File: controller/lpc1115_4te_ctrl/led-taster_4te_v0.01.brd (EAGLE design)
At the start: 66.5 x 41 mm, 29 parts, among them IC1 74HC166D, T1 BC847, T2 BC847

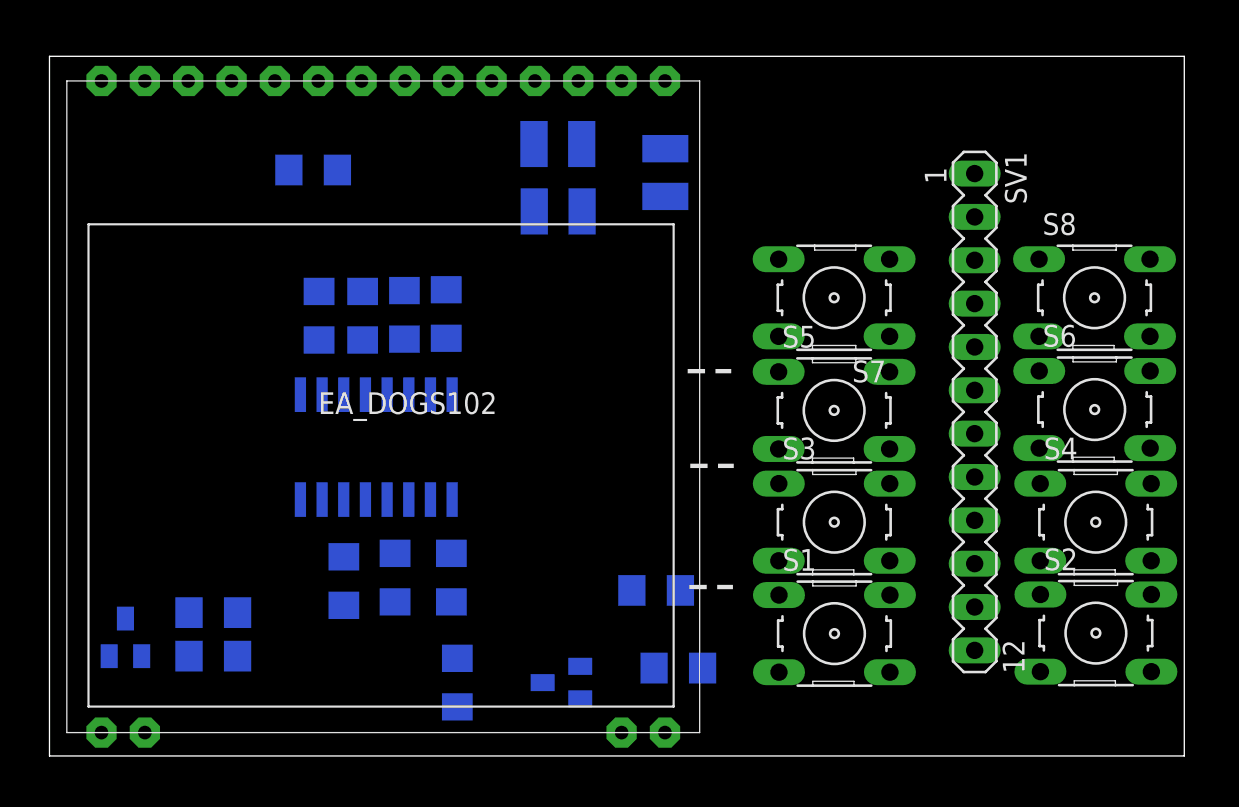
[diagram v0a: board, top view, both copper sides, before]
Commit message: LCD Taster PCB geroutet
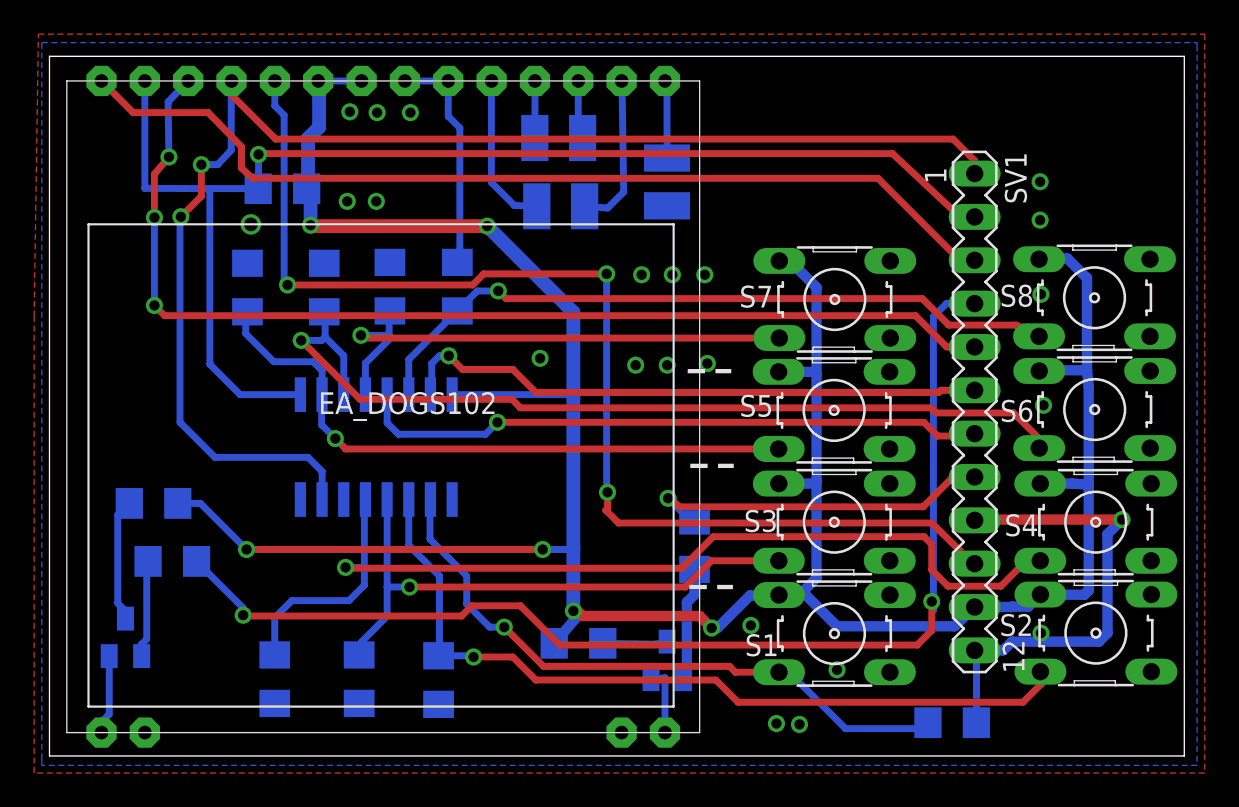
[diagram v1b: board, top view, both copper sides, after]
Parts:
- moved R2 19.0 mm to (52.9, 1.95), turned to 180 degrees
- moved R10 7.46 mm to (31.0, 6.60), turned to 180 degrees
- moved R11 7.29 mm to (6.10, 14.8)
- moved R13 7.26 mm to (37.8, 12.3), turned to 90 degrees
- moved R5 7.03 mm to (13.2, 4.50)
- moved T2 6.33 mm to (36.2, 5.60), turned to 0 degrees
- moved R4 6.31 mm to (18.1, 4.50)
- moved R12 6.05 mm to (7.20, 11.4)
- moved R3 6.05 mm to (22.8, 4.45)
- moved R6 4.51 mm to (11.6, 27.4)
- moved R7 2.79 mm to (16.1, 27.4)
- moved R1 2.11 mm to (13.7, 33.2)
- moved R8 1.86 mm to (19.9, 27.5)
- moved R9 1.73 mm to (23.9, 27.5)
- moved C3 0.56 mm to (36.2, 33.6)
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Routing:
- net +3V3: track 0.00 -> 166.5 mm, vias 0 -> 6
- net SCK: track 0.00 -> 79.7 mm, vias 0 -> 2
- net RESET: track 0.00 -> 74.8 mm, vias 0 -> 1
- net N$23: track 0.00 -> 68.3 mm, vias 0 -> 2
- net MOSI: track 0.00 -> 68.0 mm, vias 0 -> 3
- net N$26: track 0.00 -> 63.0 mm, vias 0 -> 3
- net N$9: track 0.00 -> 58.6 mm, vias 0 -> 1
- net N$14: track 0.00 -> 56.3 mm
- net N$13: track 0.00 -> 53.0 mm, vias 0 -> 1
- net N$7: track 0.00 -> 47.6 mm, vias 0 -> 1
- net N$11: track 0.00 -> 41.8 mm, vias 0 -> 1
- net GND: track 0.00 -> 40.9 mm, vias 0 -> 23
- net N$1: track 0.00 -> 37.4 mm, vias 0 -> 1
- net N$10: track 0.00 -> 37.2 mm, vias 0 -> 1
- net MISO: track 0.00 -> 37.0 mm, vias 0 -> 1
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- added copper zone on layer 1, net GND
- added copper zone on layer 16, net GND
